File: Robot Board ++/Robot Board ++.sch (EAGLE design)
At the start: 24 parts, among them IC1 FT232RQ

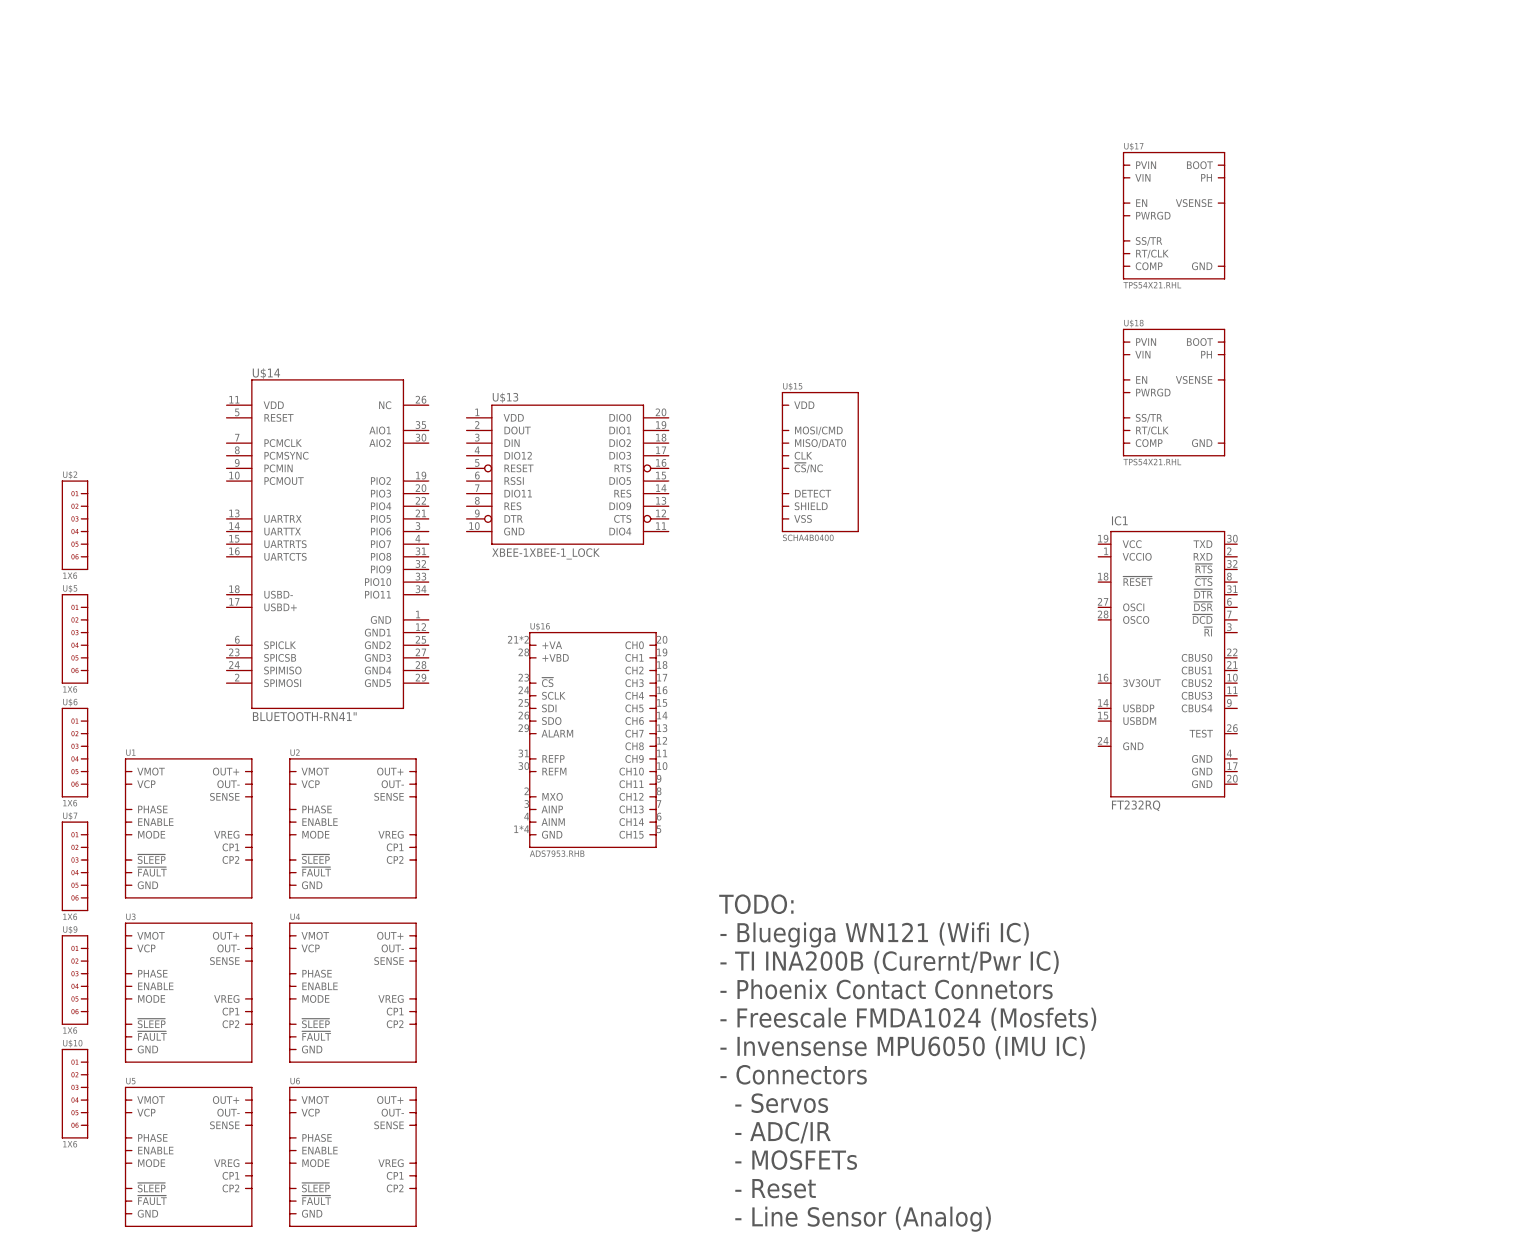
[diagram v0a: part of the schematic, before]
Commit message: Added headers for 4 Motors, 4 Quad Enc, 6 ADCs, 6 Servos, Analog Line Sensor, 4 Mosfets, 4 GPIO. Added 2 Dual Mosfet ICs, IMU IC Remved WiFi IC, FTDI IC
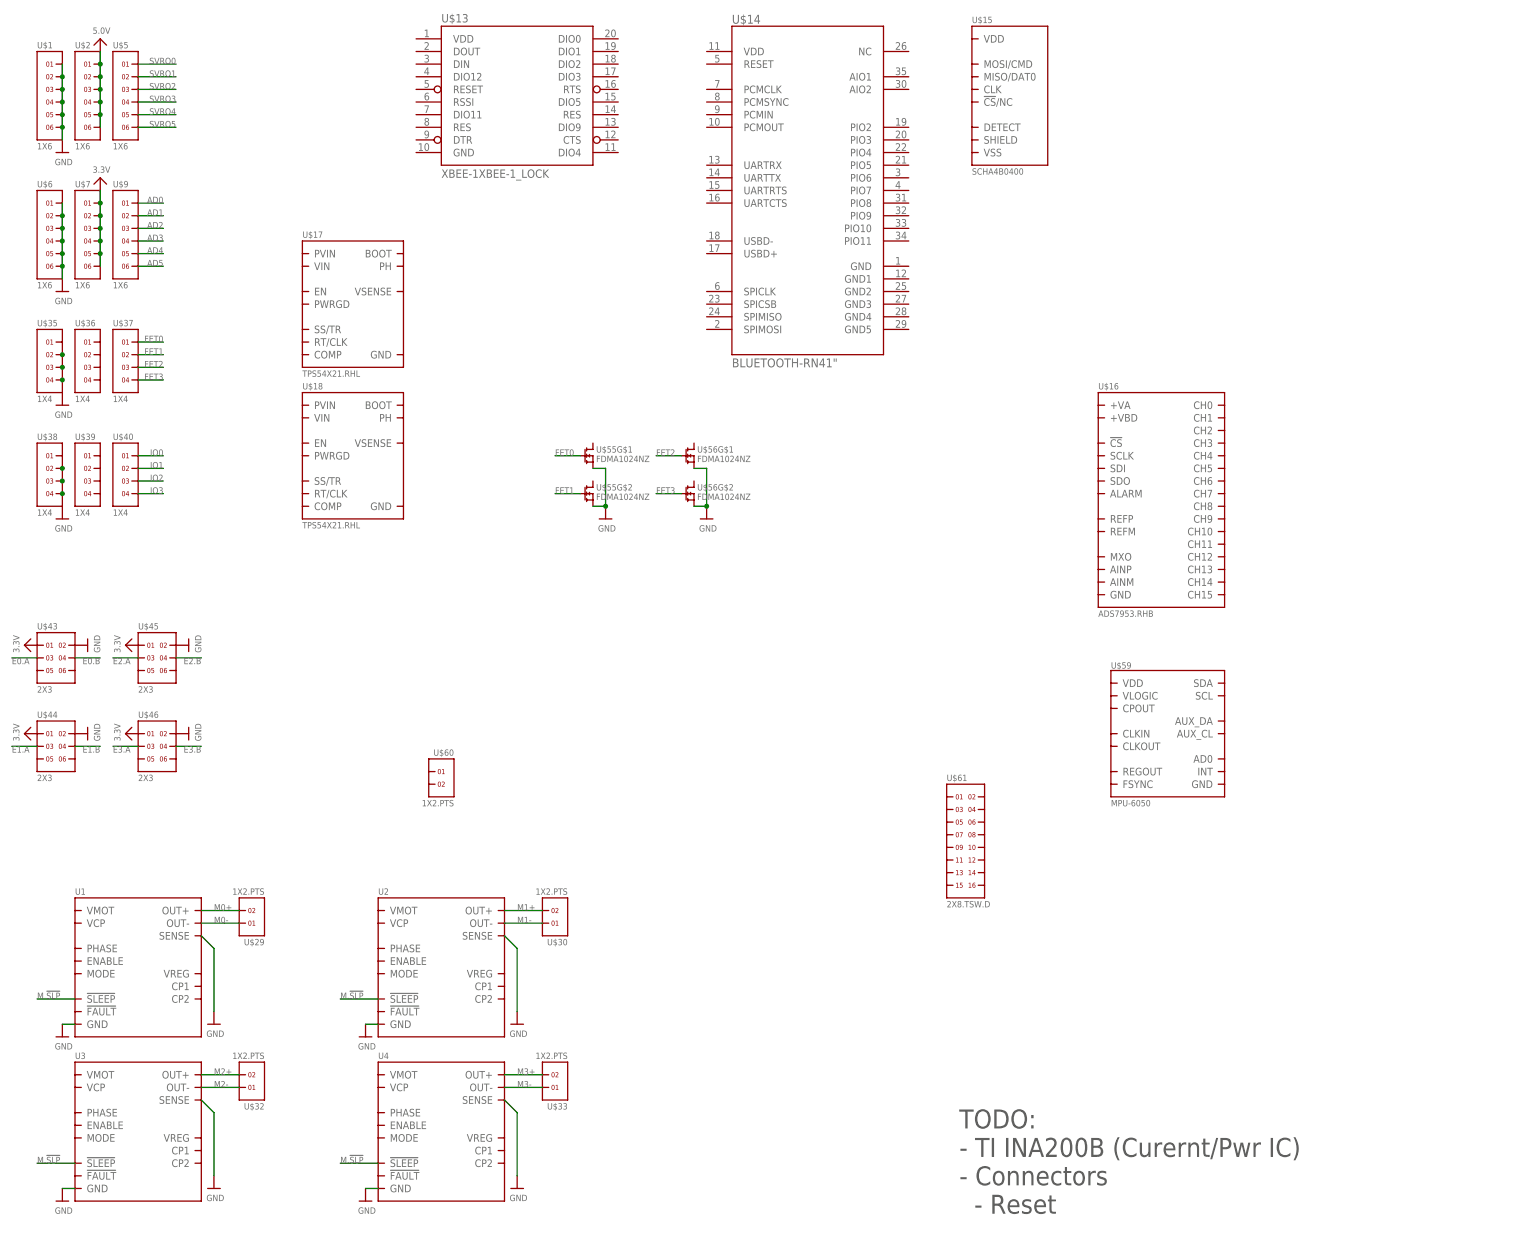
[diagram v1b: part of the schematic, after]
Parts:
- removed IC1: FT232RQ, ftdi:FT232RQ
- removed U$10: 1X6, headers(.1in):1X6
- removed U5, U6: (no value), packages(ti):DRV8800.RTY
- added U$1: 1X6, headers(.1in):1X6
- added U$29, U$30, U$32, U$33, U$60: 1X2.PTS, phoenixcontact:1X2.PTS.PLUG
- added U$35, U$36, U$37, U$38, U$39, U$40: 1X4, headers(.1in):1X4
- added U$43, U$44, U$45, U$46: 2X3, headers(.1in):2X3
- added U$55, U$56: FDMA1024NZ, freescale:FDMA1024NZ
- added U$59: MPU-6050, invensense:MPU-6050
- added U$61: 2X8.TSW.D, headers(.1in)(samtec):2X8.TSW.D
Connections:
- new net 3.3V: U$43.1, U$44.1, U$45.1, U$46.1, U$7.1, U$7.2, U$7.3, U$7.4, U$7.5, U$7.6
- new net 5.0V: U$2.1, U$2.2, U$2.3, U$2.4, U$2.5, U$2.6
- new net AD0: U$9.1
- new net AD1: U$9.2
- new net AD2: U$9.3
- new net AD3: U$9.4
- new net AD4: U$9.5
- new net AD5: U$9.6
- new net E0.A: U$43.3
- new net E0.B: U$43.4
- new net E1.A: U$44.3
- new net E1.B: U$44.4
- new net E2.A: U$45.3
- new net E2.B: U$45.4
- new net E3.A: U$46.3
- new net E3.B: U$46.4
- new net FET0: U$37.1, U$55G$1.G
- new net FET1: U$37.2, U$55G$2.G
- new net FET2: U$37.3, U$56G$1.G
- new net FET3: U$37.4, U$56G$2.G
- new net GND: U$1.1, U$1.2, U$1.3, U$1.4, U$1.5, U$1.6, U$43.2, U$44.2, U$45.2, U$46.2, U$55G$1.S, U$55G$2.S, U$56G$1.S, U$56G$2.S, U$6.1, U$6.2, U$6.3, U$6.4, U$6.5, U$6.6, U1.GND, U1.SENSE, U2.GND, U2.SENSE, U3.GND, U3.SENSE, U4.GND, U4.SENSE
- new net IO0: U$40.1
- new net IO1: U$40.2
- new net IO2: U$40.3
- new net IO3: U$40.4
- new net M.!SLP: U1.!SLEEP, U2.!SLEEP, U3.!SLEEP, U4.!SLEEP
- new net M0+: U$29.2, U1.OUT+
- new net M0-: U$29.1, U1.OUT-
- new net M1+: U$30.2, U2.OUT+
- new net M1-: U$30.1, U2.OUT-
- new net M2+: U$32.2, U3.OUT+
- new net M2-: U$32.1, U3.OUT-
- new net M3+: U$33.2, U4.OUT+
- new net M3-: U$33.1, U4.OUT-
- new net N$1: U$38.4
- new net N$2: U$38.3
- new net N$3: U$38.2
- new net N$4: U$35.4
- new net N$5: U$35.3
- new net N$6: U$35.2
- new net SVRO0: U$5.1
- new net SVRO1: U$5.2
- new net SVRO2: U$5.3
- new net SVRO3: U$5.4
- new net SVRO4: U$5.5
- new net SVRO5: U$5.6
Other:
- note added: "TODO: - TI INA200B (Curernt/Pwr IC) - Connectors - Reset"
- note removed: "TODO: - Bluegiga WN121 (Wifi IC) - TI INA200B (Curernt/Pwr IC) - Phoenix Contact Connetors - Freescale FMDA1024 (Mosfets) - Invensense MPU6050 (IMU IC) - Connectors - Servos - ADC/IR - MOSFETs - Reset - Line Sensor (Analog)"
- moved on the sheet: U$13, U$14, U$15, U$17, U$18, U$2, U$5, U$6, U$7, U$9, U1, U2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

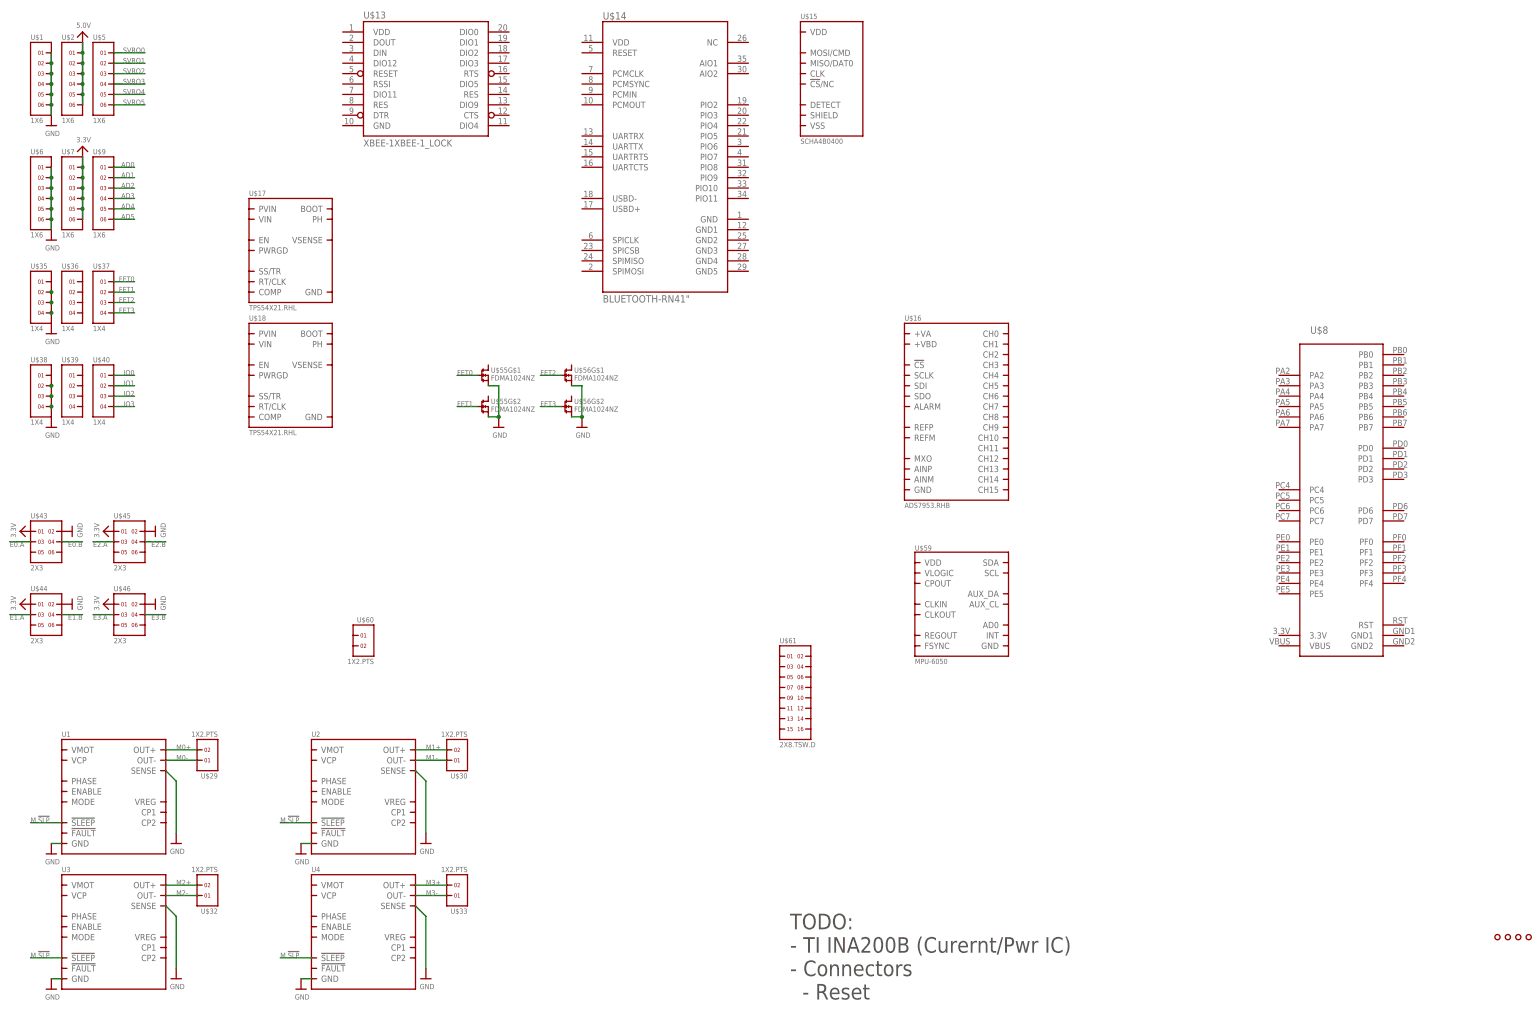
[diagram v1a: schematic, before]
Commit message: Finalized(?) board/headers layout Finalized LineSensor connector Connected ADC lines and Line Sensor to ADS7953
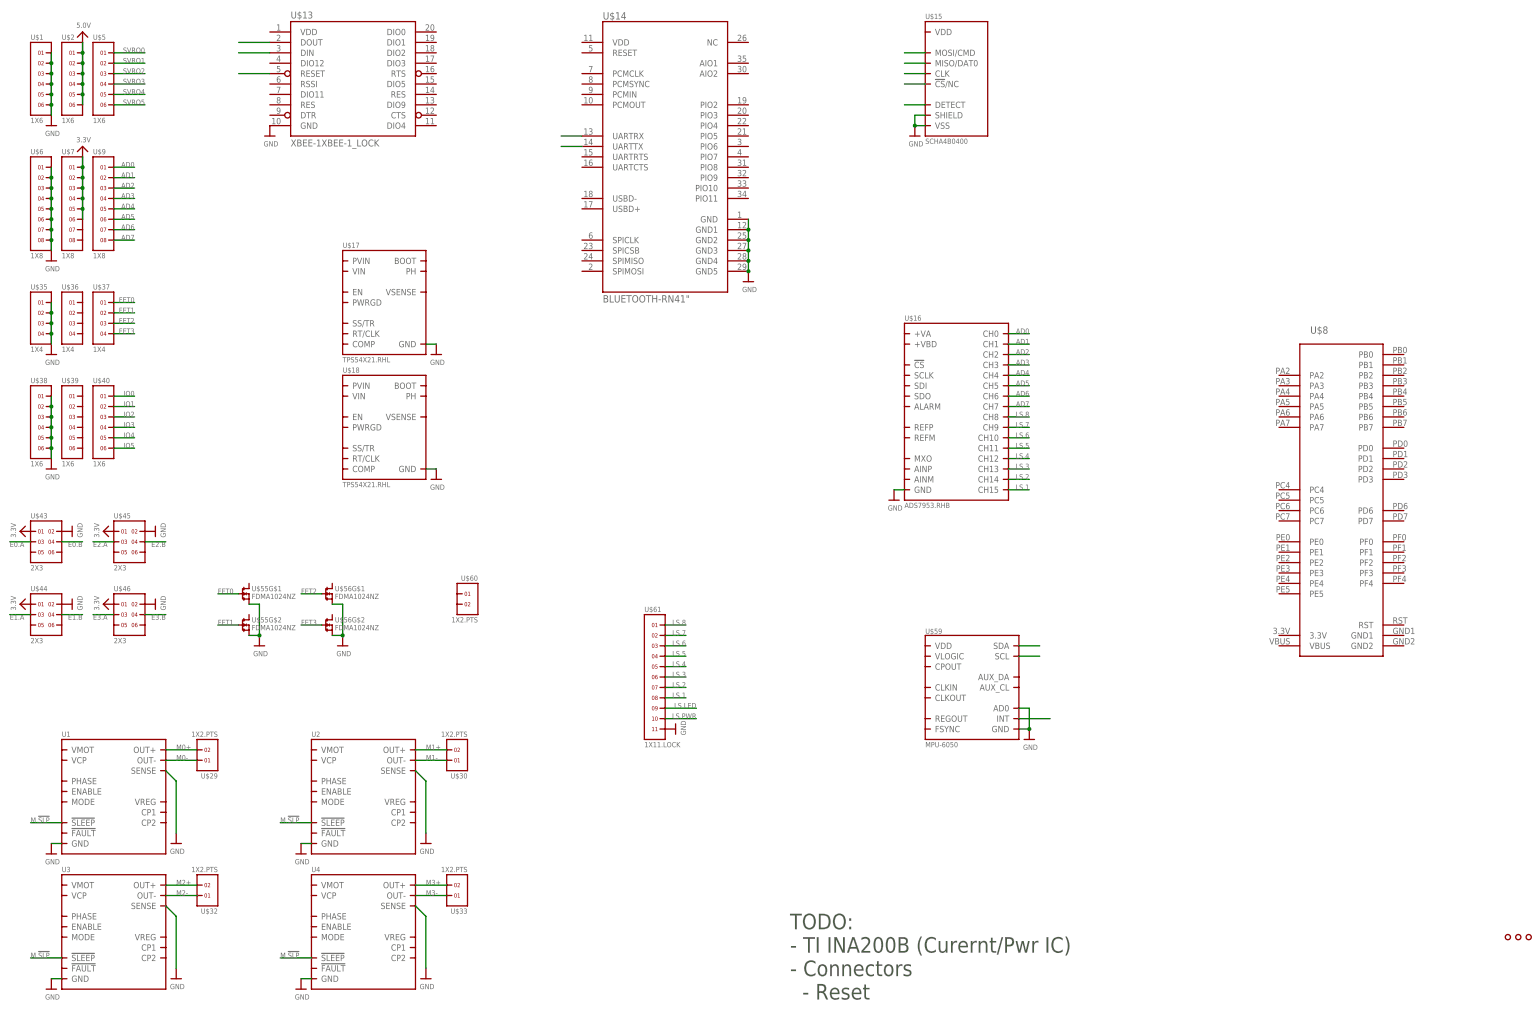
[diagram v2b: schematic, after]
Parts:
- removed U$12: HOLE.4MM, screw_holes:HOLE.4MM
- U$38, U$39, U$40: value 1X4 -> 1X6; device headers(.1in):1X4 -> headers(.1in):1X6
- U$6, U$7, U$9: value 1X6 -> 1X8; device headers(.1in):1X6 -> headers(.1in):1X8
- U$61: value 2X8.TSW.D -> 1X11.LOCK; device headers(.1in)(samtec):2X8.TSW.D -> headers(.1in):1X11.LOCK
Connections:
- removed net N$6: U$35.2
- new net AD6: U$16.CH6, U$9.7
- new net AD7: U$16.CH7, U$9.8
- new net IO4: U$40.5
- new net IO5: U$40.6
- new net LS.1: U$16.CH15, U$61.8
- new net LS.2: U$16.CH14, U$61.7
- new net LS.3: U$16.CH13, U$61.6
- new net LS.4: U$16.CH12, U$61.5
- new net LS.5: U$16.CH11, U$61.4
- new net LS.6: U$16.CH10, U$61.3
- new net LS.7: U$16.CH9, U$61.2
- new net LS.8: U$16.CH8, U$61.1
- new net LS.LED: U$61.9
- new net LS.PWR: U$61.10
- new net N$19: U$14.UARTRX
- new net N$20: U$59.INT
- new net N$21: U$14.UARTTX
- new net N$22: U$15.DETECT
- new net N$23: U$15.!CS!/NC
- new net N$24: U$15.CLK
- new net N$25: U$15.MISO/DAT0
- new net N$26: U$15.MOSI/CMD
- net AD0: now also U$16.CH0
- net AD1: now also U$16.CH1
- net AD2: now also U$16.CH2
- net AD3: now also U$16.CH3
- net AD4: now also U$16.CH4
- net AD5: now also U$16.CH5
- net GND: now also U$13.GND, U$14.GND, U$14.GND1, U$14.GND2, U$14.GND3, U$14.GND4, U$14.GND5, U$15.SHIELD, U$15.VSS, U$16.GND, U$17.GND, U$18.GND, U$35.1, U$35.2, U$35.3, U$35.4, U$38.1, U$38.2, U$38.3, U$38.4, U$38.5, U$38.6, U$59.AD0, U$59.GND, U$6.7, U$6.8, U$61.11
- net N$1: now also U$59.SDA; no longer U$38.4
- net N$2: now also U$59.SCL; no longer U$38.3
- net N$3: now also U$13.DOUT; no longer U$38.2
- net N$4: now also U$13.DIN; no longer U$35.4
- net N$5: now also U$13.RESET; no longer U$35.3
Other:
- moved on the sheet: U$13, U$15, U$17, U$18, U$35, U$36, U$37, U$55G$1, U$55G$2, U$56G$1, U$56G$2, U$59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
